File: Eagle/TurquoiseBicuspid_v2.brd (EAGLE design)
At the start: 56 x 56 mm, 19 parts, among them J0 0Ω, J1 10118192-0001LF, J2 0Ω

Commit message: added frame
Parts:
- C2: value 0.1µf -> 10µf
- renumbered J1 to USB
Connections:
- removed net N$3: HM-10.13, J0.2
- net GND: now also HM-10.13, HM-10.14, HM-10.21, HM-10.22, J0.2
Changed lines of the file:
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@@
 <element name="R6" library="resistor" package="R1206" value="10kΩ" x="2.5" y="-6.8"/>
 <element name="HM-10" library="HM-10" package="HM-10" value="HM-10BOARD" x="47.4" y="44.1"/>
-<element name="J1" library="fci_micro_usb" package="10118192-0001LF" value="10118192-0001LF" x="0" y="30.5" rot="R270"/>
+<element name="USB" library="fci_micro_usb" package="10118192-0001LF" value="10118192-0001LF" x="0" y="30.5" rot="R270"/>
 <element name="ATTINY85" library="attiny85" package="ATTINY85" value="ATTINY85SU" x="-6.2" y="-4.7"/>
-<element name="C2" library="rcl" package="C1206" value="0.1µf" x="-8.4" y="-12.7"/>
+<element name="C2" library="rcl" package="C1206" value="10µf" x="-8.4" y="-12.7"/>
 <element name="C3" library="rcl" package="C1206" value="10µf" x="-8.4" y="-18.8"/>
 </elements>
@@
 <contactref element="3.3VREG" pad="1"/>
 <contactref element="3.3VREG" pad="3"/>
-<contactref element="J1" pad="1"/>
+<contactref element="USB" pad="1"/>
 <contactref element="C3" pad="1"/>
 <wire x1="26.6799" y1="16.2" x2="26.6799" y2="18.1" width="0" layer="19" extent="1-1"/>
@@
 <wire x1="32.7" y1="11.7" x2="35.7" y2="11.7" width="0.254" layer="1"/>
 <wire x1="35.7" y1="11.7" x2="35.7" y2="15.2" width="0.254" layer="1"/>
-<contactref element="J1" pad="5"/>
+<contactref element="USB" pad="5"/>
 <contactref element="ATTINY85" pad="4"/>
 <contactref element="ATTINY85" pad="4"/>
@@
 <contactref element="C2" pad="2"/>
 <contactref element="C3" pad="2"/>
-<wire x1="19.7" y1="48.5594" x2="24.7388" y2="48.5594" width="0" layer="19" extent="1-1"/>
+<contactref element="HM-10" pad="14"/>
+<contactref element="HM-10" pad="21"/>
+<contactref element="HM-10" pad="22"/>
+<contactref element="J0" pad="2"/>
+<contactref element="HM-10" pad="13"/>
+<wire x1="51.9" y1="24.225" x2="53.4" y2="26.1" width="0" layer="19" extent="1-1"/>
+<wire x1="41.4" y1="24.225" x2="51.9" y2="24.225" width="0" layer="19" extent="1-1"/>
+<wire x1="39.9" y1="26.1" x2="41.4" y2="24.225" width="0" layer="19" extent="1-1"/>
+<wire x1="35.7" y1="23.4" x2="39.9" y2="26.1" width="0" layer="19" extent="1-1"/>
 <wire x1="29.26" y1="25.9" x2="28.1" y2="25.9" width="0" layer="19" extent="1-1"/>
-<wire x1="22.7" y1="26.28" x2="24.9" y2="23.4" width="0" layer="19" extent="1-1"/>
+<wire x1="35.7" y1="16.768" x2="35.7" y2="19.612" width="0" layer="19" extent="1-1"/>
+<wire x1="35.7" y1="15.2" x2="35.7" y2="16.768" width="0" layer="19" extent="1-1"/>
 <wire x1="3.0988" y1="1.8594" x2="0.8" y2="4.1" width="0" layer="19" extent="1-1"/>
 <wire x1="46.4688" y1="1.8594" x2="49.7" y2="1.8594" width="0" layer="19" extent="1-1"/>
+<wire x1="24.7388" y1="48.5594" x2="19.7" y2="48.5594" width="0" layer="19" extent="1-1"/>
 <wire x1="-4.295" y1="-8.03" x2="3.0988" y2="1.8594" width="0" layer="19" extent="1-1"/>
 <wire x1="-7" y1="-12.7" x2="-4.295" y2="-8.03" width="0" layer="19" extent="1-1"/>
@@
 <wire x1="39.9" y1="44.1" x2="3.922" y2="-2.9" width="0" layer="19" extent="1-1"/>
 </signal>
-<signal name="N$3">
-<contactref element="J0" pad="2"/>
-<contactref element="HM-10" pad="13"/>
-<wire x1="35.7" y1="16.768" x2="39.9" y2="26.1" width="0" layer="19" extent="1-1"/>
-</signal>
 </signals>

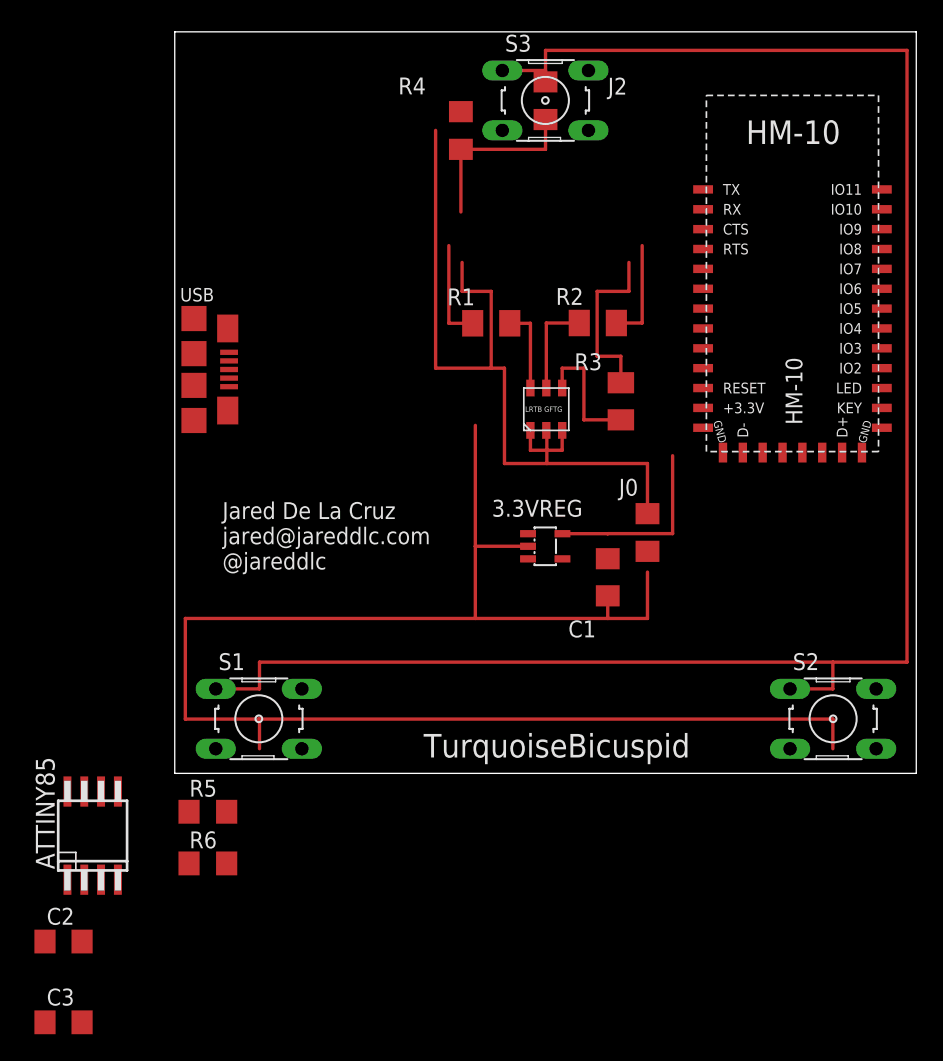
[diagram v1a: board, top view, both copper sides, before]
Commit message: fixed pulldown resistor
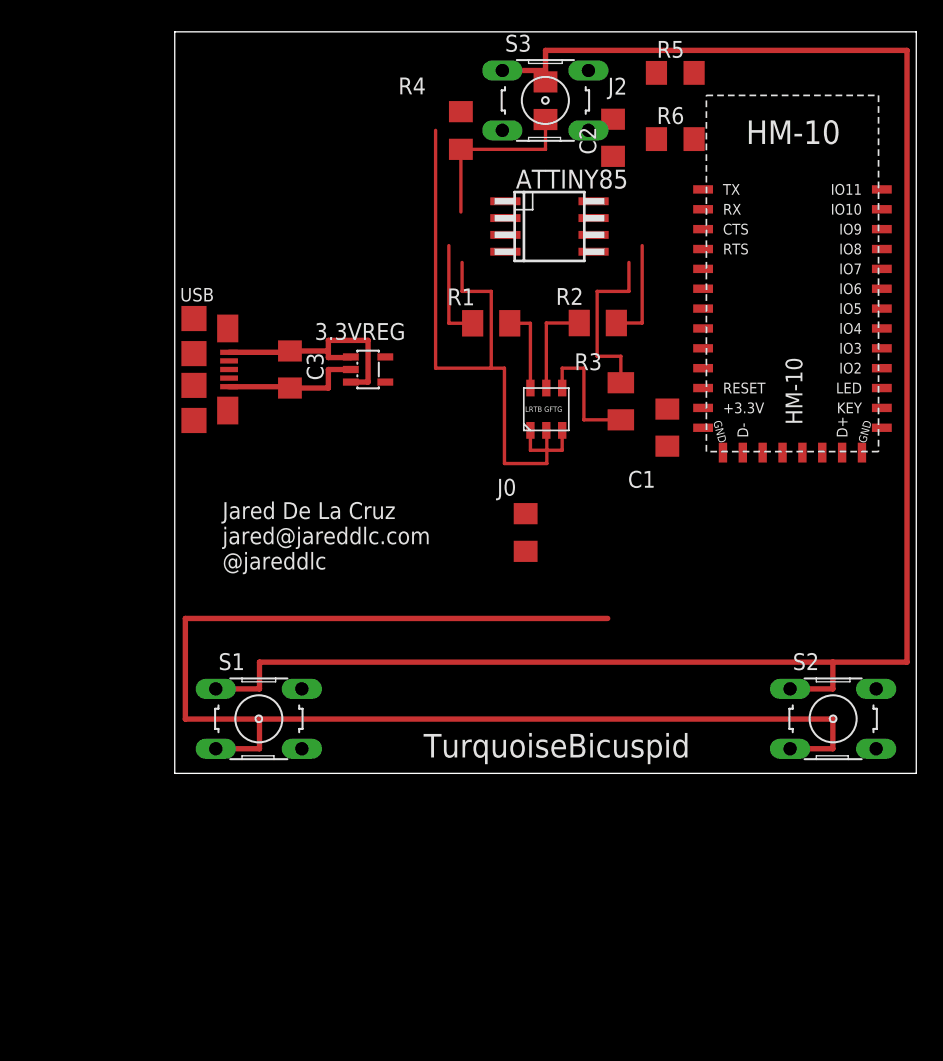
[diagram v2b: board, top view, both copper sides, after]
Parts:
- C2: value 10µf -> 0.1µf
- moved C2 73.5 mm to (33.1, 48.0), turned to 90 degrees
- moved R5 66.0 mm to (37.8, 52.9)
- moved R6 65.1 mm to (37.8, 47.9)
- moved ATTINY85 57.5 mm to (28.3, 41.3), turned to 270 degrees
- moved C3 52.2 mm to (8.70, 30.5), turned to 270 degrees
- moved 3.3VREG 18.9 mm to (14.6, 30.5)
- moved C1 12.2 mm to (37.2, 26.1)
- moved J0 9.20 mm to (26.5, 18.2)
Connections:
- removed net N$1: HM-10.1, R5.2
- removed net N$2: HM-10.2, R6.2
- net BT_RX: now also HM-10.2, R6.2; no longer R6.1
- net BT_TX: now also HM-10.1, R5.2; no longer R5.1
- net GND: now also R5.1, R6.1
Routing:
- net GND: track 182.7 -> 161.7 mm
- net 5V: track 0.00 -> 18.0 mm
- net 3.3V: track 14.2 -> 0.00 mm

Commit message: connecting routes
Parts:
- moved J0 12.3 mm to (17.3, 26.4), turned to 0 degrees
- moved R6 6.70 mm to (37.8, 41.2), turned to 270 degrees
- moved R5 6.28 mm to (38.8, 46.7), turned to 270 degrees
- moved C1 3.91 mm to (37.5, 22.2)
- moved HM-10 3.01 mm to (47.6, 41.1)
- moved C2 2.83 mm to (35.1, 46.0)
- moved ATTINY85 0.98 mm to (28.7, 40.4)
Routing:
- net 3.3V: track 0.00 -> 90.0 mm
- net GND: track 161.7 -> 245.6 mm
- net A3: track 23.1 -> 28.3 mm
- net A1: track 14.1 -> 18.7 mm
- net RESET: track 152.8 -> 156.7 mm
- net A2: track 15.2 -> 18.4 mm

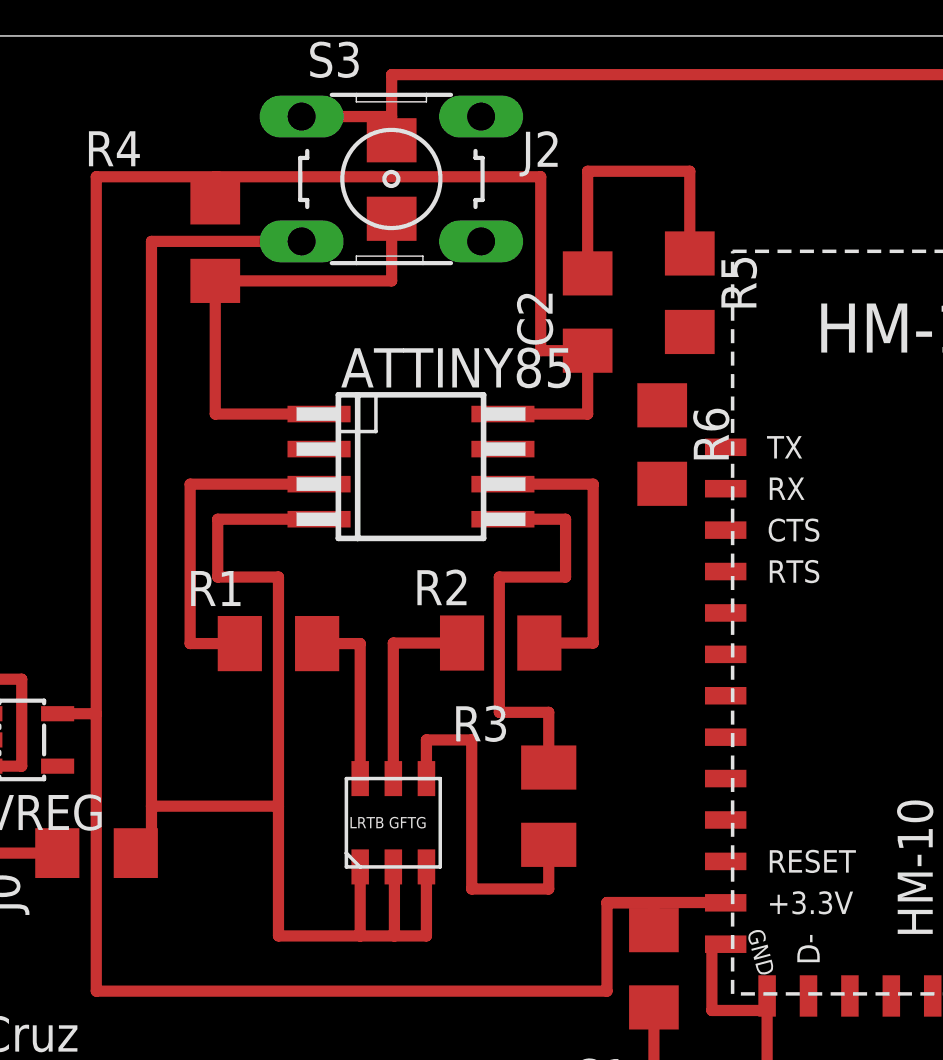
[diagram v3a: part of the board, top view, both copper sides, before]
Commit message: re-routed pins for RX & TX
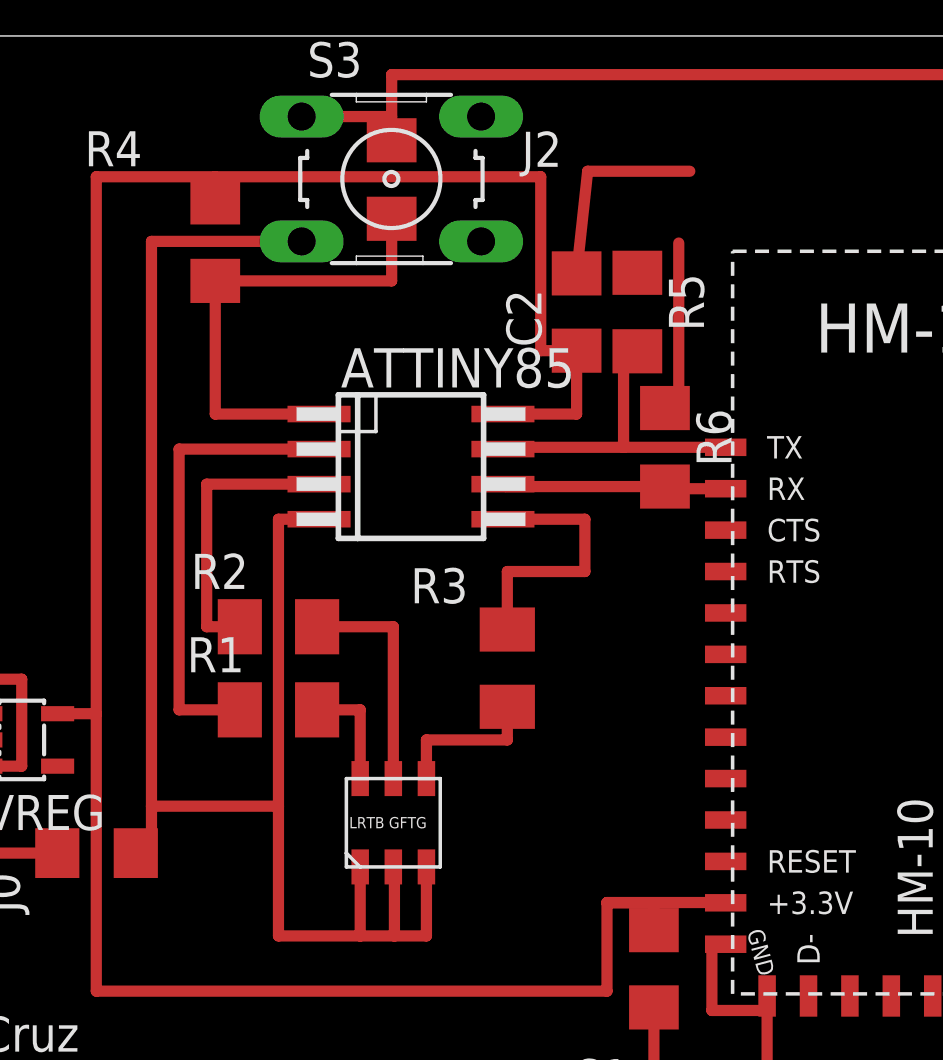
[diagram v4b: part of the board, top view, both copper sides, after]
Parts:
- moved R2 8.07 mm to (23.9, 34.6)
- moved R3 5.22 mm to (32.2, 33.1)
- moved R1 2.40 mm to (23.9, 31.6)
- moved R5 2.02 mm to (36.9, 46.0)
- moved C2 0.40 mm to (34.7, 46.0)
- moved R6 0.14 mm to (37.9, 41.1)
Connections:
- net A1: now also ATTINY85.2; no longer ATTINY85.3
- net A2: now also ATTINY85.3; no longer ATTINY85.6
- net BT_RX: now also ATTINY85.6; no longer ATTINY85.2
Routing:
- net A3: track 28.3 -> 15.3 mm
- net BT_TX: track 0.00 -> 11.8 mm
- net BT_RX: track 0.00 -> 8.49 mm
- net A1: track 18.7 -> 20.8 mm
- net GND: track 245.6 -> 244.4 mm
- net 3.3V: track 90.0 -> 89.2 mm
